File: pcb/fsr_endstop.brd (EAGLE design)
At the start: 38.1 x 38.1 mm, 33 parts, among them U1 ATTINY461

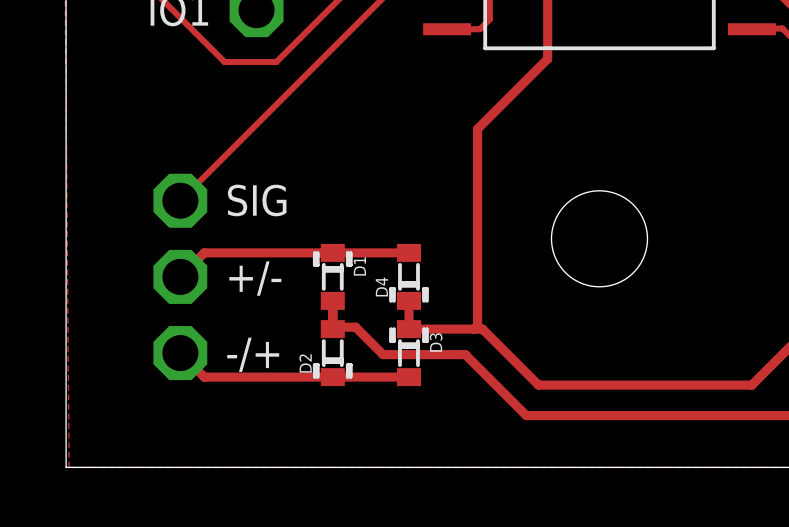
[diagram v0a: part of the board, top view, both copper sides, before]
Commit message: Reverse polarity of diodes
Diodes were backwards in the schematic for the bridge rectifier.
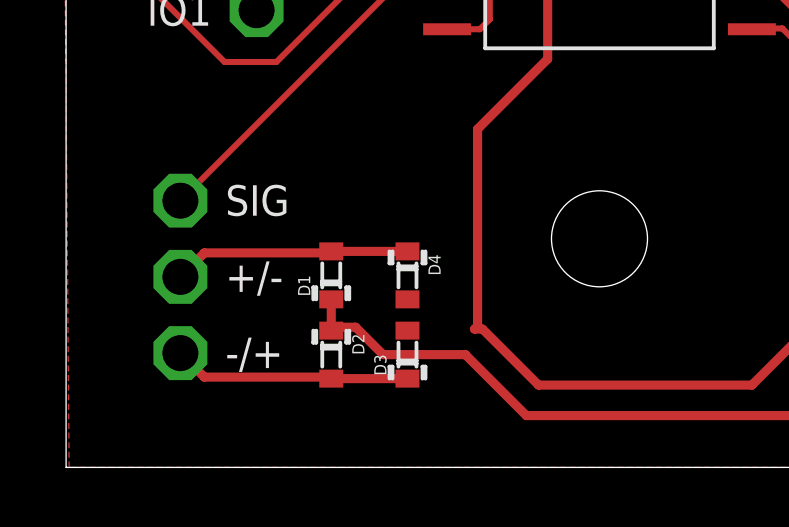
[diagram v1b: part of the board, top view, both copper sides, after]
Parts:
- moved D2 0.07 mm to (21.5, 16.5), turned to 270 degrees
- moved D3 0.07 mm to (24.1, 16.5), turned to 90 degrees
- moved D1 0.07 mm to (21.5, 19.1), turned to 90 degrees
- moved D4 0.07 mm to (24.1, 19.1), turned to 270 degrees
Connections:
- removed net N$4: +/-.P$1, D1.-, D4.+
- new net N$24: +/-.P$1, D1.+, D4.-
- net GND: now also D3.+, D4.+; no longer D3.-, D4.-
- net N$3: now also D2.+, D3.-; no longer D2.-, D3.+
- net V+: now also D1.-, D2.-; no longer D1.+, D2.+
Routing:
- net N$4: track 7.95 -> 0.00 mm
- net N$24: track 0.00 -> 7.95 mm
- net GND: track 121.5 -> 118.4 mm
- net V+: track 118.6 -> 118.0 mm
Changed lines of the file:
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@@
 <element name="FSR3A" library="_sg_lib" package="PIN_1.2MM" value="PIN1.2MM" x="44.45" y="27.94" rot="R180"/>
 <element name="AVR1" library="_sg_misc" package="AVR6" value="AVR6" x="21.59" y="45.72" rot="R180"/>
-<element name="D1" library="_sg_lib" package="0603_DIODE" value="" x="21.59" y="19.05" rot="R270"/>
-<element name="D2" library="_sg_lib" package="0603_DIODE" value="" x="21.59" y="16.51" rot="R90"/>
-<element name="D3" library="_sg_lib" package="0603_DIODE" value="" x="24.13" y="16.51" rot="R270"/>
-<element name="D4" library="_sg_lib" package="0603_DIODE" value="" x="24.13" y="19.05" rot="R90"/>
+<element name="D1" library="_sg_lib" package="0603_DIODE" value="" x="21.5392" y="19.1008" rot="R90"/>
+<element name="D2" library="_sg_lib" package="0603_DIODE" value="" x="21.5392" y="16.4592" rot="R270"/>
+<element name="D3" library="_sg_lib" package="0603_DIODE" value="" x="24.0792" y="16.4592" rot="R90"/>
+<element name="D4" library="_sg_lib" package="0603_DIODE" value="" x="24.0792" y="19.1008" rot="R270"/>
 <element name="C1" library="_sg_lib" package="0603" value="1uF" x="22.86" y="33.02" rot="R90"/>
 <element name="LED1" library="_sg_lib" package="0603_DIODE" value="LED0603" x="38.1" y="17.78" rot="R90"/>
@@
 <signals>
 <signal name="N$3">
-<contactref element="D3" pad="+"/>
-<contactref element="D2" pad="-"/>
 <contactref element="-/+" pad="P$1"/>
-<wire x1="24.13" y1="15.71" x2="21.59" y2="15.71" width="0.3048" layer="1"/>
-<wire x1="21.59" y1="15.71" x2="17.31" y2="15.71" width="0.3048" layer="1"/>
 <wire x1="17.31" y1="15.71" x2="16.51" y2="16.51" width="0.3048" layer="1"/>
-</signal>
-<signal name="N$4">
-<contactref element="+/-" pad="P$1"/>
-<contactref element="D1" pad="-"/>
-<contactref element="D4" pad="+"/>
-<wire x1="24.13" y1="19.85" x2="21.59" y2="19.85" width="0.3048" layer="1"/>
-<wire x1="21.59" y1="19.85" x2="17.31" y2="19.85" width="0.3048" layer="1"/>
-<wire x1="17.31" y1="19.85" x2="16.51" y2="19.05" width="0.3048" layer="1"/>
+<contactref element="D2" pad="+"/>
+<wire x1="17.31" y1="15.71" x2="21.5392" y2="15.71" width="0.3048" layer="1"/>
+<wire x1="21.5392" y1="15.71" x2="21.5392" y2="15.6592" width="0.3048" layer="1"/>
+<contactref element="D3" pad="-"/>
+<wire x1="21.5392" y1="15.6592" x2="24.0792" y2="15.6592" width="0.3048" layer="1"/>
 </signal>
 <signal name="V+">
-<contactref element="D2" pad="+"/>
-<contactref element="D1" pad="+"/>
 <contactref element="U1" pad="P$15"/>
 <contactref element="C1" pad="2"/>
@@
 <contactref element="R7" pad="2"/>
 <contactref element="VCC" pad="P$1"/>
-<wire x1="21.59" y1="18.25" x2="21.59" y2="17.31" width="0.3048" layer="1"/>
 <wire x1="25.4" y1="33.655" x2="23.025" y2="33.655" width="0.3048" layer="1"/>
 <wire x1="23.025" y1="33.655" x2="22.86" y2="33.82" width="0.3048" layer="1"/>
@@
 <wire x1="17.3736" y1="37.3888" x2="17.3736" y2="40.2336" width="0.3048" layer="1"/>
 <wire x1="17.3736" y1="40.2336" x2="20.32" y2="43.18" width="0.3048" layer="1"/>
-<wire x1="21.59" y1="18.25" x2="21.59" y2="17.4244" width="0.3048" layer="1"/>
-<wire x1="21.59" y1="17.4244" x2="21.5392" y2="17.3736" width="0.3048" layer="1"/>
-<wire x1="21.5392" y1="17.3736" x2="22.352" y2="17.3736" width="0.3048" layer="1"/>
 <wire x1="22.352" y1="17.3736" x2="23.2664" y2="16.4592" width="0.3048" layer="1"/>
 <wire x1="23.2664" y1="16.4592" x2="26.0096" y2="16.4592" width="0.3048" layer="1"/>
@@
 <wire x1="49.06" y1="30.48" x2="49.06" y2="17.9704" width="0.3048" layer="1"/>
 <wire x1="49.06" y1="17.9704" x2="45.5168" y2="14.4272" width="0.3048" layer="1"/>
+<contactref element="D1" pad="-"/>
+<contactref element="D2" pad="-"/>
+<wire x1="22.352" y1="17.3736" x2="21.5392" y2="17.3736" width="0.3048" layer="1"/>
+<wire x1="21.5392" y1="17.3736" x2="21.5392" y2="17.2592" width="0.3048" layer="1"/>
+<wire x1="21.5392" y1="17.2592" x2="21.5392" y2="18.3008" width="0.3048" layer="1"/>
 </signal>
 <signal name="GND">
-<contactref element="D4" pad="-"/>
-<contactref element="D3" pad="-"/>
 <contactref element="C1" pad="1"/>
 <contactref element="U1" pad="P$6"/>
@@
 <contactref element="LED3" pad="-"/>
 <contactref element="LED4" pad="-"/>
-<wire x1="24.13" y1="18.25" x2="24.13" y2="17.31" width="0.3048" layer="1"/>
-<wire x1="24.13" y1="17.31" x2="26.3144" y2="17.31" width="0.3048" layer="1"/>
 <wire x1="26.3144" y1="17.31" x2="26.5812" y2="17.31" width="0.3048" layer="1"/>
 <wire x1="26.5812" y1="17.31" x2="28.448" y2="15.4432" width="0.3048" layer="1"/>
@@
 <vertex x="12.4968" y="49.8856"/>
 </polygon>
+<contactref element="D4" pad="+"/>
+<contactref element="D3" pad="+"/>
 </signal>
 <signal name="N$1">
@@
 <wire x1="22.225" y1="34.925" x2="19.05" y2="38.1" width="0.3048" layer="1"/>
 </signal>
+<signal name="N$24">
+<contactref element="D4" pad="-"/>
+<contactref element="D1" pad="+"/>
+<contactref element="+/-" pad="P$1"/>
+<wire x1="17.31" y1="19.85" x2="16.51" y2="19.05" width="0.3048" layer="1"/>
+<wire x1="17.31" y1="19.85" x2="21.5392" y2="19.85" width="0.3048" layer="1"/>
+<wire x1="21.5392" y1="19.85" x2="21.5392" y2="19.9008" width="0.3048" layer="1"/>
+<wire x1="21.5392" y1="19.9008" x2="24.0792" y2="19.9008" width="0.3048" layer="1"/>
+</signal>
 </signals>
